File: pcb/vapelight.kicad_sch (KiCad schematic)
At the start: 42 parts, among them J1 USB_A, J2 Conn_01x01_Socket, J3 Conn_01x01_Socket, J4 Conn_01x01_Socket, J5 Conn_01x01_Socket, Q1 FS8205A, SW1 SW_Push, U1 DW01A, U2 LTC4054ES5-4.2, U3 LM27313XMF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

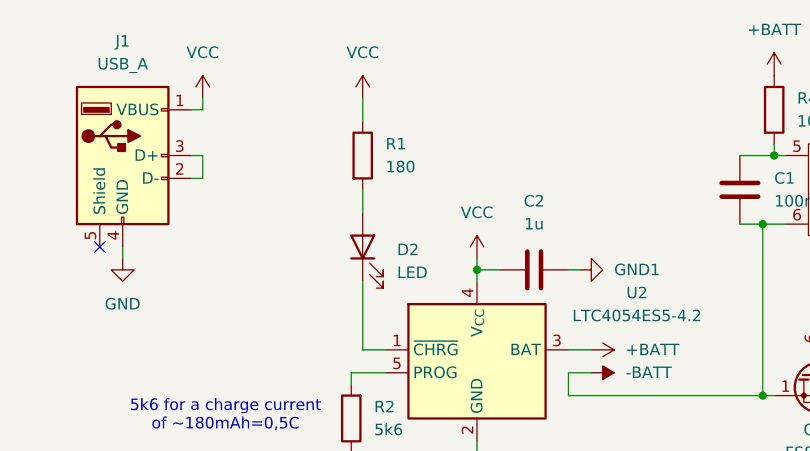
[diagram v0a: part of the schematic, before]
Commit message: Revision F
– less bright charge LED
– higher button
– different sizes of panelized fabrication outputs
- minor fixes
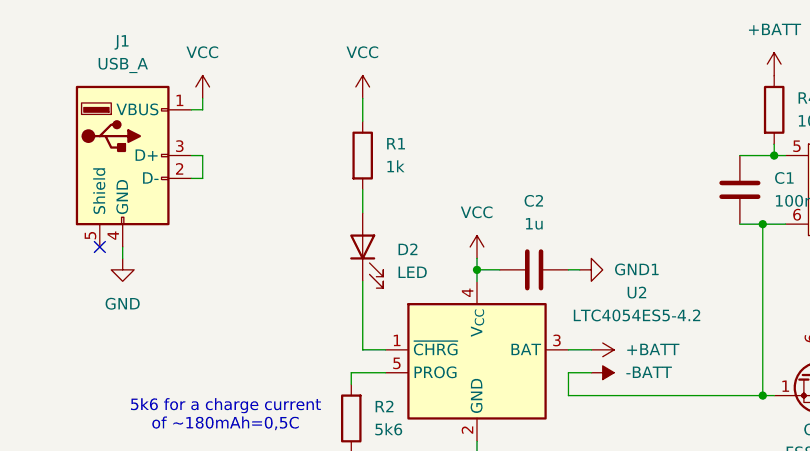
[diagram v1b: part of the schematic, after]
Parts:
- R1: value 180 -> 1k; LCSC C22828 -> C21190
- SW1: LCSC C571338 -> C318886
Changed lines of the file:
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@@
 	(title_block
 		(title "vapelight")
-		(date "2025-03-05")
-		(rev "E")
+		(date "2025-05-22")
+		(rev "F")
 		(company "SBYD")
 	)
@@
 			)
 		)
-		(property "Value" "180"
+		(property "Value" "1k"
 			(at 67.31 41.9099 0)
 			(effects
@@
 			)
 		)
-		(property "LCSC" "C22828"
+		(property "LCSC" "C21190"
 			(at 64.77 40.64 0)
 			(effects
@@
 			)
 		)
-		(property "LCSC" "C571338"
+		(property "LCSC" "C318886"
 			(at 43.18 173.99 0)
 			(effects
